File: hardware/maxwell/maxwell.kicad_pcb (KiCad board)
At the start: 2 copper layers, 129.5 x 59.7 mm, 90 parts, among them J1 Canbus 1, J2 Canbus 2, J3 Neopixel, J4 Boot Selection Jumper, J5 Charger Output, J6 Programmer, J7 Dynamo Input, J8 USB Input, J9 Battery, Q1 BSS138, Q2 Q_NMOS_GDS, Q3 Q_PMOS_GDS, U1 MCP2515-E/ST-SOIC, U10 LT1529, U11 TPS2514, U2 SN65HVD233, U3 ITEAD_HC-05, U4 SIM800L_5-pin, U5 BOOST_BOARD, U6 STT3P2UH7, U7 STM32F103RETx, U8 TLP188, U9 Buck Regulator, Y1 16M, Y2 8M, Y3 32.768k

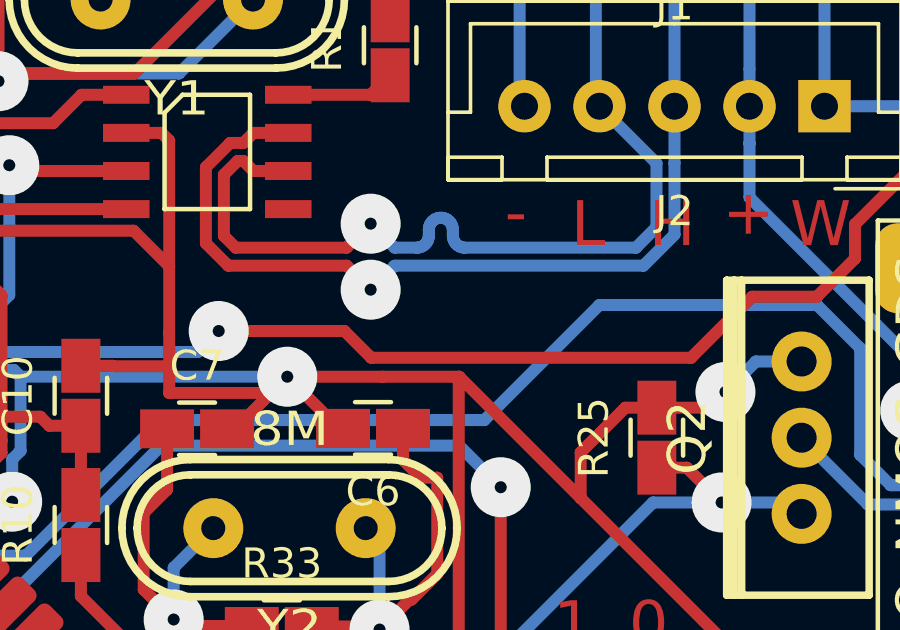
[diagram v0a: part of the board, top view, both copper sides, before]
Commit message: Adding CANBus termination resistors.
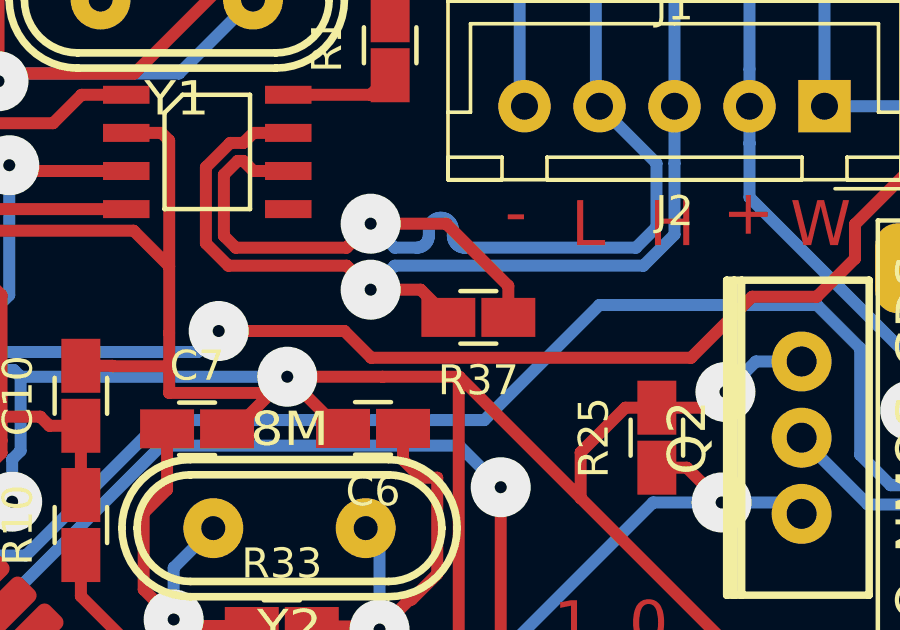
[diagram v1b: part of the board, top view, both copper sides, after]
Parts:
- added R37: 120, coddingtonbear/coddingtonbear.pretty:0805_Milling, F.Cu at (168.8, 89.8)
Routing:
- net /CAN-: track 33.3 -> 39.8 mm
- net /CAN+: track 33.9 -> 36.9 mm
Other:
- net class Default: trace_width 0.25 -> 0.4
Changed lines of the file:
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@@
-(kicad_pcb (version 20170123) (host pcbnew no-vcs-found-e2505cb~60~ubuntu16.04.1)
+(kicad_pcb (version 20170920) (host pcbnew "(2017-09-25 revision 6e440ff)-master")
   (general
     (thickness 1.6)
     (drawings 25)
-    (tracks 1438)
+    (tracks 1443)
     (zones 0)
-    (modules 90)
+    (modules 91)
     (nets 128)
   )
@@
   )
   (setup
-    (last_trace_width 0.25)
+    (last_trace_width 0.4)
     (trace_clearance 0.2)
     (zone_clearance 0.508)
@@
   (net_class Default "This is the default net class."
     (clearance 0.2)
-    (trace_width 0.25)
+    (trace_width 0.4)
     (via_dia 2)
     (via_drill 0.4)
@@
     (add_net ~ENABLE_USB_OUT)
   )
+  (module coddingtonbear/coddingtonbear.pretty:0805_Milling (layer F.Cu)
+    (at 168.80154 89.84234 180)
+    (descr "Resistor SMD 0805, reflow soldering, Vishay (see dcrcw.pdf)")
+    (tags "resistor 0805")
+    (attr smd)
+    (fp_text reference R37 (at 0 -2.1 180) (layer F.SilkS)
+      (effects (font (size 1 1) (thickness 0.15)))
+    )
+    (fp_text value 120 (at 0 2.1 180) (layer F.Fab)
+      (effects (font (size 1 1) (thickness 0.15)))
+    )
+    (fp_line (start -0.6 -0.875) (end 0.6 -0.875) (layer F.SilkS) (width 0.15))
+    (fp_line (start 0.6 0.875) (end -0.6 0.875) (layer F.SilkS) (width 0.15))
+    (pad 2 smd rect (at 1 0 180) (size 1.8 1.3) (layers F.Cu F.Paste F.Mask)
+      (net 105 /CAN+))
+    (pad 1 smd rect (at -1 0 180) (size 1.8 1.3) (layers F.Cu F.Paste F.Mask)
+      (net 104 /CAN-))
+    (model Resistors_SMD.3dshapes/R_0805.wrl
+      (at (xyz 0 0 0))
+      (scale (xyz 1 1 1))
+      (rotate (xyz 0 0 0))
+    )
+  )
   (module kicad-castellated-breakouts:QFP64-1.27MM-CASTELLATED (layer F.Cu)
     (at 146.556078 108.694616 225)
@@
   (segment (start 126.658952 96.377) (end 127.515029 97.233077) (width 0.4) (layer F.Cu) (net 32))
   (segment (start 125.222 96.377) (end 126.658952 96.377) (width 0.4) (layer F.Cu) (net 32))
+  (segment (start 165.212272 86.719628) (end 167.728828 86.719628) (width 0.4) (layer F.Cu) (net 104))
+  (segment (start 167.728828 86.719628) (end 169.80154 88.79234) (width 0.4) (layer F.Cu) (net 104))
+  (segment (start 169.80154 88.79234) (end 169.80154 89.84234) (width 0.4) (layer F.Cu) (net 104))
+  (segment (start 165.212272 88.919628) (end 166.878828 88.919628) (width 0.4) (layer F.Cu) (net 105))
+  (segment (start 166.878828 88.919628) (end 167.80154 89.84234) (width 0.4) (layer F.Cu) (net 105))
   (segment (start 111.24946 79.29116) (end 112.86314 79.29116) (width 0.4) (layer F.Cu) (net 127))
   (segment (start 112.86314 79.29116) (end 113.4016 78.7527) (width 0.4) (layer F.Cu) (net 127))

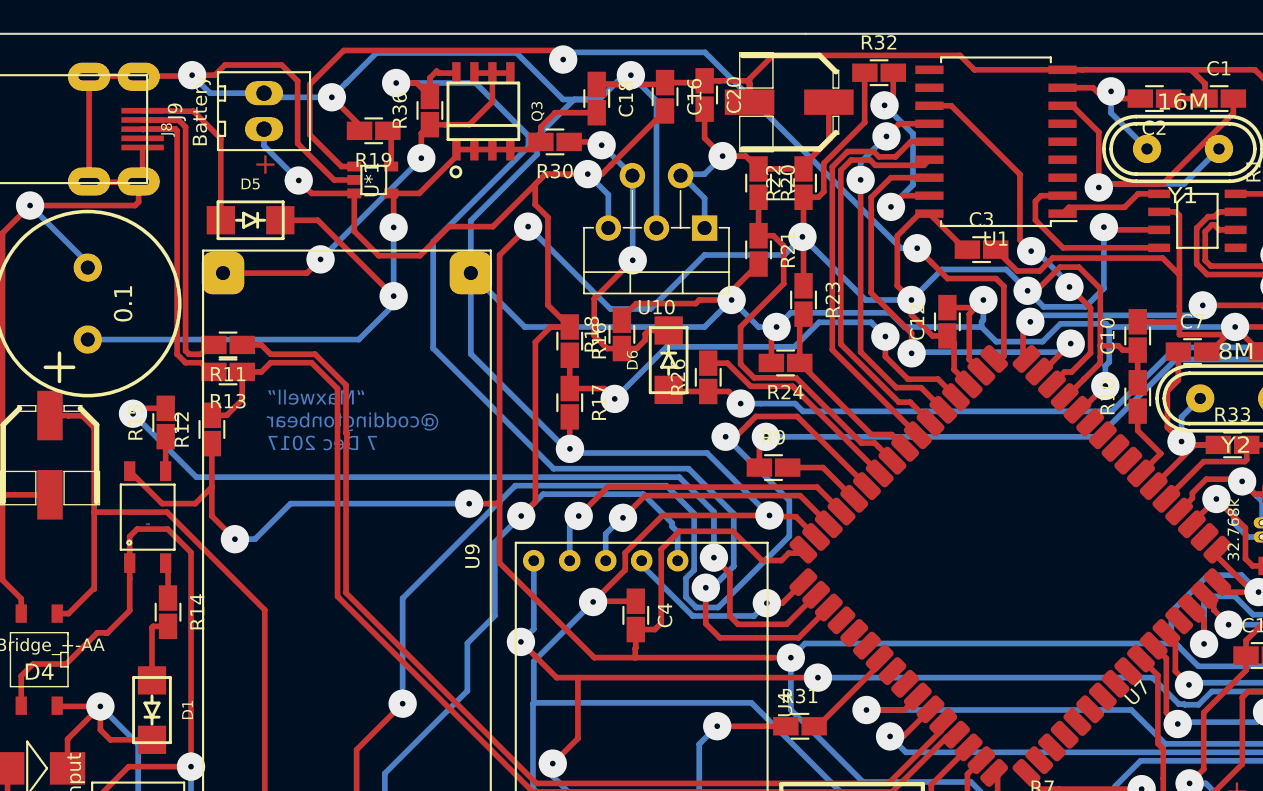
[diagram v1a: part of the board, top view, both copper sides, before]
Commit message: Move current measurement to battery side of ldo; obviously.  Also, remove now-redundant second current sense trace.
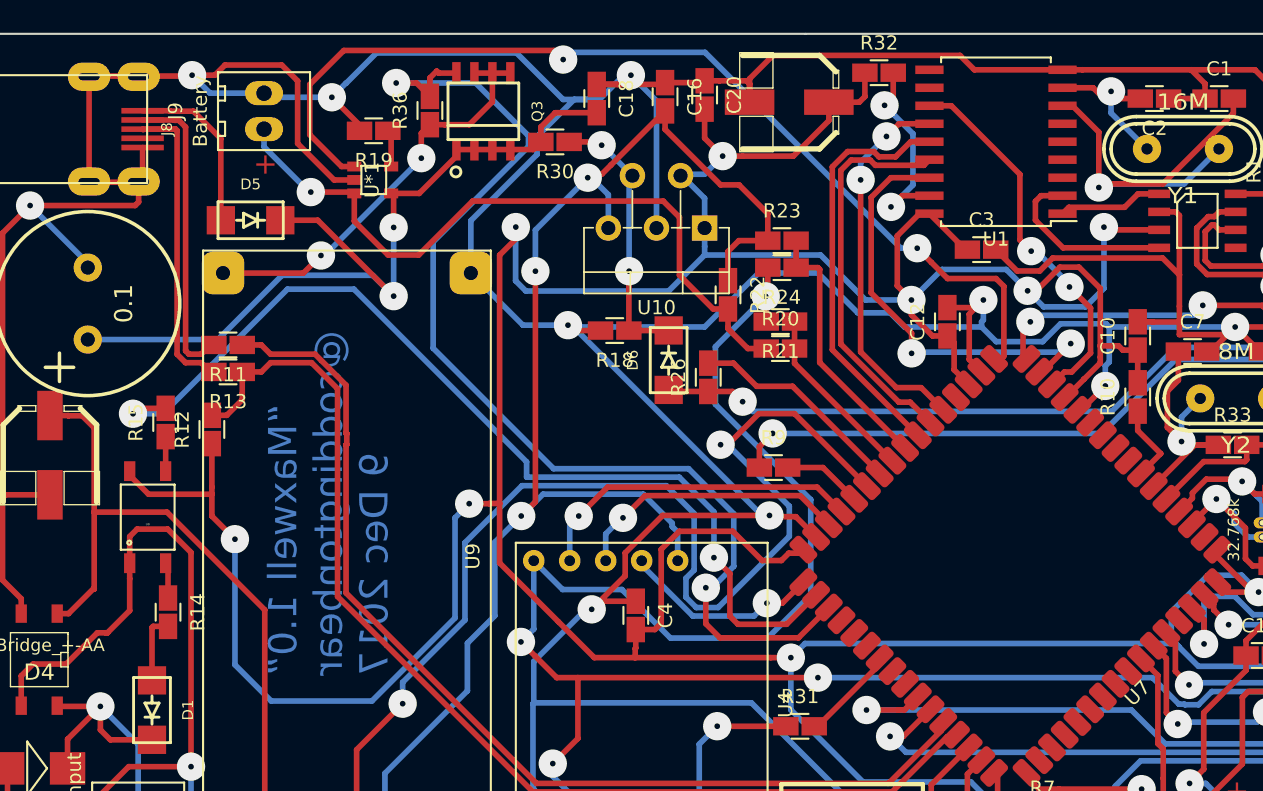
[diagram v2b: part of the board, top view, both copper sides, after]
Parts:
- removed R16: 4.7k, coddingtonbear/coddingtonbear.pretty:0805_Milling
- removed R17: 10k, coddingtonbear/coddingtonbear.pretty:0805_Milling
- moved R20 11.8 mm to (130.3, 93.3), turned to 0 degrees
- moved R22 9.52 mm to (126.6, 89.6), turned to 270 degrees
- moved R24 6.74 mm to (130.4, 87.6)
- moved R21 5.29 mm to (130.3, 91.4), turned to 180 degrees
- moved R23 4.46 mm to (130.4, 85.7), turned to 0 degrees
- moved R18 0.58 mm to (118.6, 92.1), turned to 180 degrees
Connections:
- net AC renamed DYNAMO_AC
- net AC_NEUTRAL renamed DYNAMO_NEUTRAL
- net CURRENT_SENSE_2 renamed CURRENT_SENSE
- C19 pad 1: Net-(C19-Pad1) -> +3V3
- C20 pad 2: Net-(C19-Pad1) -> +3V3
- J9 pad 1: +BATT -> Net-(J9-Pad1)
- R20 pad 1: Net-(C19-Pad1) -> Net-(J9-Pad1)
- R20 pad 2: CURRENT_SENSE_1 -> BATT_VOLTAGE
- R21 pad 1: CURRENT_SENSE_1 -> BATT_VOLTAGE
- R21 pad 2: GND -> GNDPWR
- R22 pad 1: +3V3 -> +BATT
- R22 pad 2: Net-(C19-Pad1) -> Net-(J9-Pad1)
- R23 pad 1: +3V3 -> +BATT
- R24 pad 2: GND -> GNDPWR
- U*1 pad 3: +BATT -> Net-(J9-Pad1)
- U10 pad 1: Net-(C19-Pad1) -> +3V3
- U10 pad 2: Net-(C19-Pad1) -> +3V3
- U7 pad 20: BATT_VOLTAGE -> Net-(U7-Pad20)
- U7 pad 25: CURRENT_SENSE_1 -> BATT_VOLTAGE
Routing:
- net GNDPWR: track 227.9 -> 280.2 mm, vias 4 -> 5
- net Net-(J9-Pad1): track 0.00 -> 50.2 mm, vias 0 -> 1
- net +3V3: track 352.5 -> 381.8 mm
- net CURRENT_SENSE_1: track 28.4 -> 0.00 mm
- net GND: track 664.9 -> 639.5 mm, vias 21 -> 19
- net Net-(C19-Pad1): track 23.5 -> 0.00 mm, vias 1 -> 0
- net BATT_VOLTAGE: track 35.5 -> 13.3 mm, vias 2 -> 0
- net +BATT: track 266.5 -> 252.1 mm
- net SPEED: track 61.8 -> 69.7 mm
- net Net-(D6-Pad1): track 24.7 -> 19.8 mm
- net CURRENT_SENSE: track 14.2 -> 18.7 mm
- net /Power/+Dynamo: track 58.6 -> 59.4 mm
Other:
- net class Default: trace_width 0.4 -> 0.25
- board text added: "“Maxwell 1.0” @coddingtonbear 9 Dec 2017"
- board text removed: "“Maxwell” @coddingtonbear 7 Dec 2017"

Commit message: Updating schematic/layout to latest kicad version.
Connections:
- C2 pad 1: GND -> Net-(C2-Pad1)
- U6 pad 2: Net-(J5-Pad1) -> Net-(U6-Pad2)
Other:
- net class Default: clearance 0.2 -> 0.25; trace_width 0.25 -> 0.4
- rule trace_clearance: 0.2 -> 0.25
